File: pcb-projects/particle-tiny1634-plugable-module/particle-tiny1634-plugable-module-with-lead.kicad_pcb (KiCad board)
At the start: 2 copper layers, 41.3 x 47.6 mm, 33 parts, among them IC1 ATTINY1634-SU, P1 INTERFACE, P2 MCU_TEST

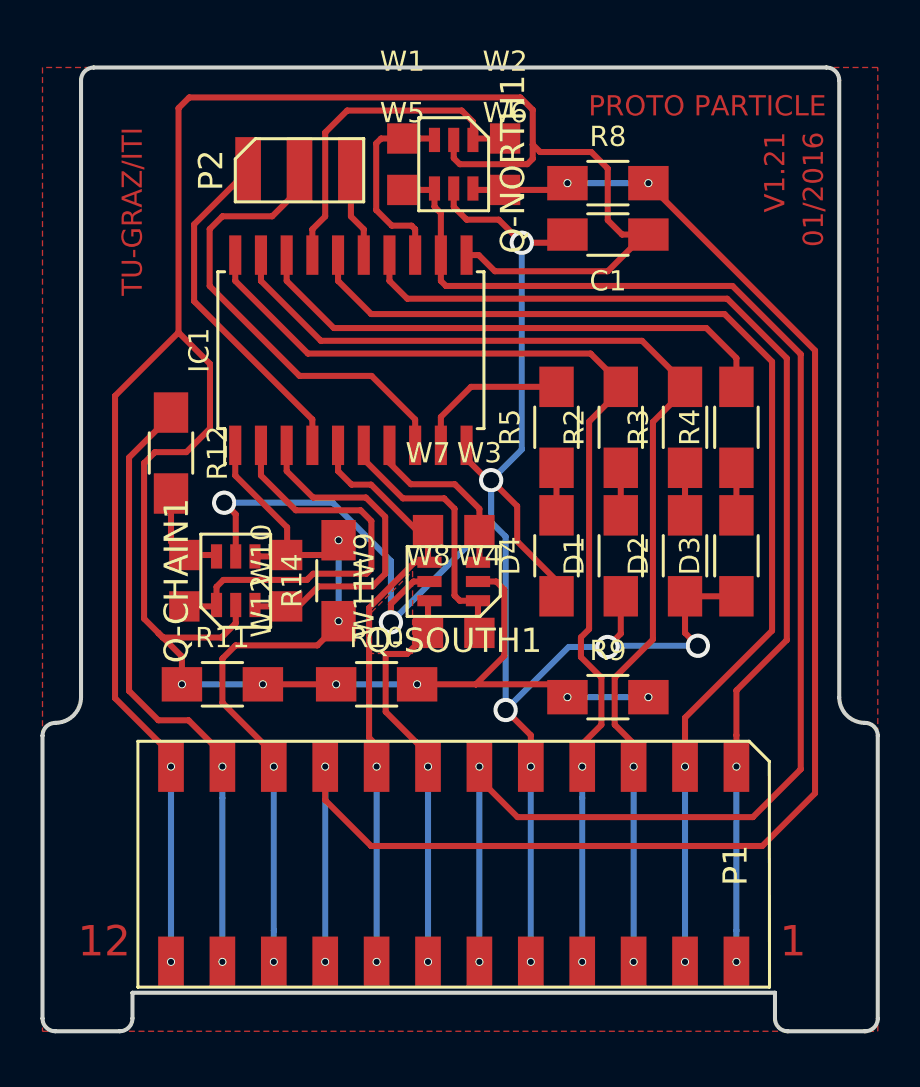
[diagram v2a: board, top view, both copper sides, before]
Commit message: minor change: updated MCU power supply decoupling and euro pcb
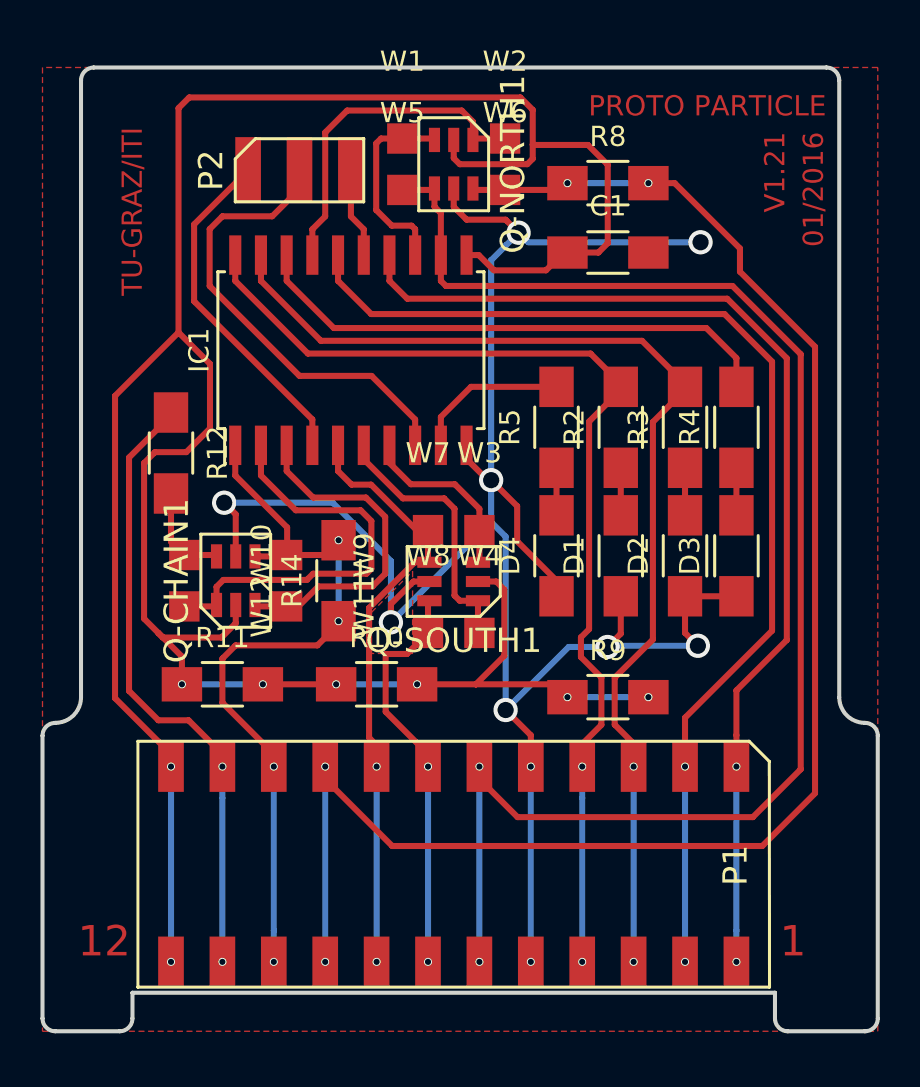
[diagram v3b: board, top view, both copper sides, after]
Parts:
- moved C1 0.89 mm to (154.9, 93.0), turned to 0 degrees
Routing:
- net GND: track 98.3 -> 105.1 mm, vias 9 -> 10
- net VCC: track 145.4 -> 142.1 mm
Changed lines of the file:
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@@
     (thickness 1.6)
     (drawings 32)
-    (tracks 351)
+    (tracks 356)
     (zones 0)
     (modules 33)
@@
   )
   (module Capacitors_SMD:C_1206_HandSoldering (layer F.Cu)
-    (at 154.94 92.075 180)
+    (at 154.94 92.964)
     (descr "Capacitor SMD 1206, hand soldering")
     (tags "capacitor 1206")
     (attr smd)
-    (fp_text reference C1 (at 0 -2.3 180) (layer F.SilkS)
-      (effects (font (size 1 1) (thickness 0.15)))
-    )
-    (fp_text value 100nF (at 0 2.3 180) (layer F.Fab)
+    (fp_text reference C1 (at 0 -2.3) (layer F.SilkS)
+      (effects (font (size 1 1) (thickness 0.15)))
+    )
+    (fp_text value 100nF (at 0 2.3) (layer F.Fab)
       (effects (font (size 1 1) (thickness 0.15)))
     )
@@
     (fp_line (start 1 -1.025) (end -1 -1.025) (layer F.SilkS) (width 0.15))
     (fp_line (start -1 1.025) (end 1 1.025) (layer F.SilkS) (width 0.15))
-    (pad 1 smd rect (at -2 0 180) (size 2 1.6) (layers F.Cu F.Paste F.Mask)
+    (pad 1 smd rect (at -2 0) (size 2 1.6) (layers F.Cu F.Paste F.Mask)
       (net 17 VCC))
-    (pad 2 smd rect (at 2 0 180) (size 2 1.6) (layers F.Cu F.Paste F.Mask)
+    (pad 2 smd rect (at 2 0) (size 2 1.6) (layers F.Cu F.Paste F.Mask)
       (net 1 GND))
     (model Capacitors_SMD.3dshapes/C_1206_HandSoldering.wrl
@@
   (gr_line (start 165.735 83.82) (end 129.54 83.82) (layer Edge.Cuts) (width 0.2))
   (gr_line (start 166.37 114.935) (end 166.37 84.455) (layer Edge.Cuts) (width 0.2))
-  (segment (start 150.683271 92.479859) (end 152.535141 92.479859) (width 0.3) (layer F.Cu) (net 1))
-  (segment (start 152.535141 92.479859) (end 152.94 92.075) (width 0.3) (layer F.Cu) (net 1))
+  (segment (start 149.926194 91.383638) (end 150.526193 91.983637) (width 0.3) (layer F.Cu) (net 1))
+  (segment (start 149.882415 91.339859) (end 149.926194 91.383638) (width 0.3) (layer F.Cu) (net 1))
+  (segment (start 147.959859 91.339859) (end 149.882415 91.339859) (width 0.3) (layer F.Cu) (net 1))
+  (segment (start 147.32 90.7) (end 147.959859 91.339859) (width 0.3) (layer F.Cu) (net 1))
+  (segment (start 147.32 89.8) (end 147.32 90.7) (width 0.3) (layer F.Cu) (net 1))
+  (segment (start 149.170598 93.339232) (end 149.926194 92.583636) (width 0.3) (layer B.Cu) (net 1))
+  (segment (start 149.170598 104.2119) (end 149.170598 93.339232) (width 0.3) (layer B.Cu) (net 1))
+  (segment (start 159.51815 92.455664) (end 150.99822 92.455664) (width 0.3) (layer B.Cu) (net 1))
+  (segment (start 149.926194 92.583636) (end 150.526193 91.983637) (width 0.3) (layer B.Cu) (net 1))
+  (via (at 150.526193 91.983637) (size 1.2) (drill 0.8) (layers F.Cu B.Cu) (net 1))
+  (segment (start 150.99822 92.455664) (end 150.526193 91.983637) (width 0.3) (layer B.Cu) (net 1))
+  (via (at 159.51815 92.455664) (size 1.2) (drill 0.8) (layers F.Cu B.Cu) (net 1))
   (segment (start 135.976871 105.326818) (end 141.339591 105.326818) (width 0.3) (layer B.Cu) (net 1))
   (segment (start 141.339591 105.326818) (end 144.217311 108.204538) (width 0.3) (layer B.Cu) (net 1))
@@
   (segment (start 149.170598 104.2119) (end 149.170598 106.283802) (width 0.3) (layer B.Cu) (net 1))
   (segment (start 149.170598 106.283802) (end 144.217311 111.237089) (width 0.3) (layer B.Cu) (net 1))
-  (segment (start 150.683271 92.479859) (end 150.683271 102.699227) (width 0.3) (layer B.Cu) (net 1))
-  (segment (start 150.683271 102.699227) (end 149.170598 104.2119) (width 0.3) (layer B.Cu) (net 1))
   (via (at 149.885 115.57) (size 1.2) (drill 0.8) (layers F.Cu B.Cu) (net 1))
   (segment (start 151.13 118.365) (end 151.13 116.815) (width 0.3) (layer F.Cu) (net 1) (status 10))
@@
   (segment (start 146.12 109.22) (end 145.330998 109.22) (width 0.3) (layer F.Cu) (net 1) (status 10))
   (via (at 144.217311 111.237089) (size 1.2) (drill 0.8) (layers F.Cu B.Cu) (net 1))
-  (segment (start 147.32 89.8) (end 147.32 90.7) (width 0.3) (layer F.Cu) (net 1) (status 10))
-  (segment (start 147.959859 91.339859) (end 149.543271 91.339859) (width 0.3) (layer F.Cu) (net 1))
-  (segment (start 147.32 90.7) (end 147.959859 91.339859) (width 0.3) (layer F.Cu) (net 1))
-  (segment (start 149.543271 91.339859) (end 150.683271 92.479859) (width 0.3) (layer F.Cu) (net 1))
-  (via (at 150.683271 92.479859) (size 1.2) (drill 0.8) (layers F.Cu B.Cu) (net 1))
   (segment (start 136.549429 105.899376) (end 135.976871 105.326818) (width 0.3) (layer F.Cu) (net 1))
   (segment (start 136.549429 107.980571) (end 136.549429 105.899376) (width 0.3) (layer F.Cu) (net 1) (status 10))
@@
   (segment (start 161.29 103.6) (end 161.29 105.95) (width 0.3) (layer F.Cu) (net 4) (status 30))
   (segment (start 152.4 103.6) (end 152.4 105.95) (width 0.3) (layer F.Cu) (net 5) (status 30))
-  (segment (start 140.97 118.365) (end 140.97 120.022562) (width 0.3) (layer F.Cu) (net 6))
-  (segment (start 143.237447 122.290009) (end 162.56901 122.290009) (width 0.3) (layer F.Cu) (net 6))
-  (segment (start 165.175077 119.683942) (end 165.175077 97.803742) (width 0.3) (layer F.Cu) (net 6))
-  (segment (start 156.94 89.568665) (end 156.94 89.535) (width 0.3) (layer F.Cu) (net 6))
-  (segment (start 140.97 120.022562) (end 143.237447 122.290009) (width 0.3) (layer F.Cu) (net 6))
   (segment (start 162.56901 122.290009) (end 165.175077 119.683942) (width 0.3) (layer F.Cu) (net 6))
-  (segment (start 165.175077 97.803742) (end 156.94 89.568665) (width 0.3) (layer F.Cu) (net 6))
+  (segment (start 158.24 89.535) (end 156.94 89.535) (width 0.3) (layer F.Cu) (net 6))
+  (segment (start 161.46484 92.75984) (end 158.24 89.535) (width 0.3) (layer F.Cu) (net 6))
+  (segment (start 144.280009 122.290009) (end 162.56901 122.290009) (width 0.3) (layer F.Cu) (net 6))
+  (segment (start 140.97 118.365) (end 140.97 118.98) (width 0.3) (layer F.Cu) (net 6))
+  (segment (start 161.46484 93.90984) (end 161.46484 92.75984) (width 0.3) (layer F.Cu) (net 6))
+  (segment (start 165.175077 97.620077) (end 161.46484 93.90984) (width 0.3) (layer F.Cu) (net 6))
+  (segment (start 165.175077 119.683942) (end 165.175077 97.620077) (width 0.3) (layer F.Cu) (net 6))
+  (segment (start 140.97 118.98) (end 144.280009 122.290009) (width 0.3) (layer F.Cu) (net 6))
   (segment (start 149.86 89.87) (end 152.605 89.87) (width 0.3) (layer F.Cu) (net 6))
   (segment (start 152.605 89.87) (end 152.94 89.535) (width 0.3) (layer F.Cu) (net 6))
@@
   (segment (start 146.685 101.088) (end 148.173 99.6) (width 0.3) (layer F.Cu) (net 16))
   (segment (start 148.173 99.6) (end 152.4 99.6) (width 0.3) (layer F.Cu) (net 16) (status 20))
-  (segment (start 156.94 92.075) (end 155.64 92.075) (width 0.3) (layer F.Cu) (net 17))
-  (segment (start 155.64 92.075) (end 154.93082 91.36582) (width 0.3) (layer F.Cu) (net 17))
-  (segment (start 154.93082 91.36582) (end 154.93082 88.811818) (width 0.3) (layer F.Cu) (net 17))
-  (segment (start 154.93082 88.811818) (end 154.115501 87.996499) (width 0.3) (layer F.Cu) (net 17))
-  (segment (start 154.115501 87.996499) (end 151.591356 87.996499) (width 0.3) (layer F.Cu) (net 17))
-  (segment (start 151.591356 87.996499) (end 151.224857 87.63) (width 0.3) (layer F.Cu) (net 17))
+  (segment (start 151.224857 87.63) (end 151.242303 87.647446) (width 0.3) (layer F.Cu) (net 17))
+  (segment (start 151.242303 87.647446) (end 153.952389 87.647446) (width 0.3) (layer F.Cu) (net 17))
+  (segment (start 153.952389 87.647446) (end 154.93082 88.625877) (width 0.3) (layer F.Cu) (net 17))
+  (segment (start 154.93082 88.625877) (end 154.93082 92.502817) (width 0.3) (layer F.Cu) (net 17))
+  (segment (start 154.93082 92.502817) (end 154.469637 92.964) (width 0.3) (layer F.Cu) (net 17))
+  (segment (start 154.469637 92.964) (end 152.94 92.964) (width 0.3) (layer F.Cu) (net 17))
+  (segment (start 147.955 93.09) (end 148.555 93.09) (width 0.3) (layer F.Cu) (net 17))
+  (segment (start 148.555 93.09) (end 149.308734 93.843734) (width 0.3) (layer F.Cu) (net 17))
+  (segment (start 149.308734 93.843734) (end 151.881477 93.843734) (width 0.3) (layer F.Cu) (net 17))
+  (segment (start 151.881477 93.843734) (end 152.761211 92.964) (width 0.3) (layer F.Cu) (net 17))
+  (segment (start 152.761211 92.964) (end 152.94 92.964) (width 0.3) (layer F.Cu) (net 17))
   (segment (start 151.224857 88.330285) (end 151.224857 87.63) (width 0.3) (layer F.Cu) (net 17))
   (segment (start 151.224857 87.63) (end 151.224857 85.912687) (width 0.3) (layer F.Cu) (net 17))
-  (segment (start 147.955 93.09) (end 148.555 93.09) (width 0.3) (layer F.Cu) (net 17))
-  (segment (start 148.555 93.09) (end 149.35411 93.88911) (width 0.3) (layer F.Cu) (net 17))
-  (segment (start 149.35411 93.88911) (end 154.933459 93.88911) (width 0.3) (layer F.Cu) (net 17))
-  (segment (start 154.933459 93.88911) (end 156.747569 92.075) (width 0.3) (layer F.Cu) (net 17))
-  (segment (start 156.747569 92.075) (end 156.94 92.075) (width 0.3) (layer F.Cu) (net 17))
   (segment (start 147.32 87.4) (end 147.32 88.3) (width 0.3) (layer F.Cu) (net 17))
   (segment (start 150.955142 88.6) (end 151.224857 88.330285) (width 0.3) (layer F.Cu) (net 17))

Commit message: elongated leads
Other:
- board size 41.3 x 47.6 mm -> 41.3 x 48.3 mm
